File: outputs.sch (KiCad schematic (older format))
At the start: 51 parts, among them J2 USB_B_Micro, J3 HDMI_A_1.4, J4 FH26W-45S-0.3SHW(60), J5 Conn_02x16_Odd_Even, J6 Conn_01x02, Q1 AO3400, SW1 Up, SW2 Down, SW3 Left, SW4 Right, SW5 A, SW6 B, SW7 Select, SW8 Start, U10 NS8002

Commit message: Proto 1
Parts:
- renumbered C54 to C34, C36 to C35, C37 to C36, C38 to C37, C39 to C38, C40 to C39, C55 to C40, C56 to C44, C44 to C45, C45 to C46, C2 to C47, D2 to D3, D3 to D4, J6 to J3, J3 to J4, J4 to J5, J5 to J6, R14 to R25, R15 to R26, R16 to R27, R34 to R28, R17 to R29, R18 to R30, R35 to R31, R19 to R32, R20 to R33, R21 to R34, R22 to R35, R23 to R36, R24 to R37, R25 to R38, R26 to R39, R27 to R40, TP2 to TP12, TP3 to TP13, TP4 to TP14, TP5 to TP15
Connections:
- wire segments 161 -> 162
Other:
- note added: "Note: 100R is too little: the unit resets (5V overload?)"
- note added: "[38,39,40]=[im2,im1,im0]\n[0,0,0]=DBI type-B 18-bit"

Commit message: New design
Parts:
- added J10, J9: Conn_01x02_Male, Connector_PinHeader_2.54mm:PinHeader_1x02_P2.54mm_Vertical, symbol Connector:Conn_01x02_Male
- added J7, J8: Conn_02x03_Odd_Even, Connector_PinSocket_2.54mm:PinSocket_2x03_P2.54mm_Vertical, symbol Connector_Generic:Conn_02x03_Odd_Even
- SW1, SW2, SW3, SW4, SW5, SW6, SW7, SW8: footprint Button_Switch_THT:SW_PUSH_6mm -> Button_Switch_SMD:SW_Push_1P1T_NO_6x6mm_H9.5mm
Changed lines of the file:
@@
 EESchema Schematic File Version 4
 LIBS:hadbadge2019-cache
-EELAYER 26 0
+EELAYER 29 0
 EELAYER END
 $Descr A4 11693 8268
@@
 F 0 "SW1" H 9850 4300 50  0000 C CNN
 F 1 "Up" H 10150 4300 50  0000 C CNN
-F 2 "Button_Switch_THT:SW_PUSH_6mm" H 9350 4450 50  0001 C CNN
+F 2 "Button_Switch_SMD:SW_Push_1P1T_NO_6x6mm_H9.5mm" H 9350 4450 50  0001 C CNN
 F 3 "" H 9350 4450 50  0001 C CNN
 	1    9350 4250
@@
 F 0 "SW2" H 9850 4500 50  0000 C CNN
 F 1 "Down" H 10150 4500 50  0000 C CNN
-F 2 "Button_Switch_THT:SW_PUSH_6mm" H 9350 4650 50  0001 C CNN
+F 2 "Button_Switch_SMD:SW_Push_1P1T_NO_6x6mm_H9.5mm" H 9350 4650 50  0001 C CNN
 F 3 "" H 9350 4650 50  0001 C CNN
 	1    9350 4450
@@
 F 0 "SW3" H 9850 4700 50  0000 C CNN
 F 1 "Left" H 10150 4700 50  0000 C CNN
-F 2 "Button_Switch_THT:SW_PUSH_6mm" H 9350 4850 50  0001 C CNN
+F 2 "Button_Switch_SMD:SW_Push_1P1T_NO_6x6mm_H9.5mm" H 9350 4850 50  0001 C CNN
 F 3 "" H 9350 4850 50  0001 C CNN
 	1    9350 4650
@@
 F 0 "SW4" H 9850 4900 50  0000 C CNN
 F 1 "Right" H 10150 4900 50  0000 C CNN
-F 2 "Button_Switch_THT:SW_PUSH_6mm" H 9350 5050 50  0001 C CNN
+F 2 "Button_Switch_SMD:SW_Push_1P1T_NO_6x6mm_H9.5mm" H 9350 5050 50  0001 C CNN
 F 3 "" H 9350 5050 50  0001 C CNN
 	1    9350 4850
@@
 F 0 "SW5" H 9850 5100 50  0000 C CNN
 F 1 "A" H 10150 5100 50  0000 C CNN
-F 2 "Button_Switch_THT:SW_PUSH_6mm" H 9350 5250 50  0001 C CNN
+F 2 "Button_Switch_SMD:SW_Push_1P1T_NO_6x6mm_H9.5mm" H 9350 5250 50  0001 C CNN
 F 3 "" H 9350 5250 50  0001 C CNN
 	1    9350 5050
@@
 F 0 "SW6" H 9850 5300 50  0000 C CNN
 F 1 "B" H 10150 5300 50  0000 C CNN
-F 2 "Button_Switch_THT:SW_PUSH_6mm" H 9350 5450 50  0001 C CNN
+F 2 "Button_Switch_SMD:SW_Push_1P1T_NO_6x6mm_H9.5mm" H 9350 5450 50  0001 C CNN
 F 3 "" H 9350 5450 50  0001 C CNN
 	1    9350 5250
@@
 F 0 "SW7" H 9850 5500 50  0000 C CNN
 F 1 "Select" H 10150 5500 50  0000 C CNN
-F 2 "Button_Switch_THT:SW_PUSH_6mm" H 9350 5650 50  0001 C CNN
+F 2 "Button_Switch_SMD:SW_Push_1P1T_NO_6x6mm_H9.5mm" H 9350 5650 50  0001 C CNN
 F 3 "" H 9350 5650 50  0001 C CNN
 	1    9350 5450
@@
 F 0 "SW8" H 9850 5700 50  0000 C CNN
 F 1 "Start" H 10150 5700 50  0000 C CNN
-F 2 "Button_Switch_THT:SW_PUSH_6mm" H 9350 5850 50  0001 C CNN
+F 2 "Button_Switch_SMD:SW_Push_1P1T_NO_6x6mm_H9.5mm" H 9350 5850 50  0001 C CNN
 F 3 "" H 9350 5850 50  0001 C CNN
 	1    9350 5650
@@
 Text Notes 1550 2850 0    50   ~ 0
 Note: 100R is too little: the unit resets (5V overload?)
+$Comp
+L Connector_Generic:Conn_02x03_Odd_Even J7
+U 1 1 5CEDF19E
+P 4000 6700
+F 0 "J7" H 4050 7017 50  0000 C CNN
+F 1 "Conn_02x03_Odd_Even" H 4050 6926 50  0000 C CNN
+F 2 "Connector_PinSocket_2.54mm:PinSocket_2x03_P2.54mm_Vertical" H 4000 6700 50  0001 C CNN
+F 3 "~" H 4000 6700 50  0001 C CNN
+	1    4000 6700
+	1    0    0    -1
+$EndComp
+$Comp
+L Connector:Conn_01x02_Male J9
+U 1 1 5CEECB55
+P 3950 7100
+F 0 "J9" H 4058 7281 50  0000 C CNN
+F 1 "Conn_01x02_Male" H 4058 7190 50  0000 C CNN
+F 2 "Connector_PinHeader_2.54mm:PinHeader_1x02_P2.54mm_Vertical" H 3950 7100 50  0001 C CNN
+F 3 "~" H 3950 7100 50  0001 C CNN
+	1    3950 7100
+	1    0    0    -1
+$EndComp
+$Comp
+L Connector_Generic:Conn_02x03_Odd_Even J8
+U 1 1 5CEEDF6E
+P 5050 6700
+F 0 "J8" H 5100 7017 50  0000 C CNN
+F 1 "Conn_02x03_Odd_Even" H 5100 6926 50  0000 C CNN
+F 2 "Connector_PinSocket_2.54mm:PinSocket_2x03_P2.54mm_Vertical" H 5050 6700 50  0001 C CNN
+F 3 "~" H 5050 6700 50  0001 C CNN
+	1    5050 6700
+	1    0    0    -1
+$EndComp
+$Comp
+L Connector:Conn_01x02_Male J10
+U 1 1 5CEEDF74
+P 5000 7100
+F 0 "J10" H 5108 7281 50  0000 C CNN
+F 1 "Conn_01x02_Male" H 5108 7190 50  0000 C CNN
+F 2 "Connector_PinHeader_2.54mm:PinHeader_1x02_P2.54mm_Vertical" H 5000 7100 50  0001 C CNN
+F 3 "~" H 5000 7100 50  0001 C CNN
+	1    5000 7100
+	1    0    0    -1
+$EndComp
 $EndSCHEMATC

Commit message: WiP for proto 2
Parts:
- J6: footprint Connector_PinSocket_2.54mm:PinSocket_2x16_P2.54mm_Vertical -> Connector_PinSocket_2.54mm:PinSocket_2x16_P2.54mm_Horizontal
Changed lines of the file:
@@
 F 0 "J6" H 6100 5467 50  0000 C CNN
 F 1 "Conn_02x16_Odd_Even" H 6100 5376 50  0000 C CNN
-F 2 "Connector_PinSocket_2.54mm:PinSocket_2x16_P2.54mm_Vertical" H 6050 4550 50  0001 C CNN
+F 2 "Connector_PinSocket_2.54mm:PinSocket_2x16_P2.54mm_Horizontal" H 6050 4550 50  0001 C CNN
 F 3 "~" H 6050 4550 50  0001 C CNN
 	1    6050 4550

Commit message: Nearly done...
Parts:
- removed J6: Conn_02x16_Odd_Even, Connector_PinSocket_2.54mm:PinSocket_2x16_P2.54mm_Horizontal, symbol Connector_Generic:Conn_02x16_Odd_Even
- added J11: Conn_02x06_Odd_Even, Connector_PinSocket_2.54mm:PinSocket_2x06_P2.54mm_Horizontal, symbol Connector_Generic:Conn_02x06_Odd_Even
- added J6: Conn_02x20_Odd_Even, Connector_PinSocket_2.54mm:PinSocket_2x20_P2.54mm_Horizontal, symbol Connector_Generic:Conn_02x20_Odd_Even
- added R48, R49, R50, R51, R52, R53: 100, Resistor_SMD:R_0603_1608Metric, symbol Device:R
- J2: footprint JeroensFootprints:USB_Micro-B_0.8mm_taobao -> JeroensFootprints:USB_Micro-B_China_MK5P
- R33, R34, R35, R36, R37, R38: value 100 -> 180
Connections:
- net labels added: FLASH_CS_EXT, FLASH_HOLD, FLASH_MISO, FLASH_MOSI, FLASH_SCK, FLASH_WP, PMODA_1, PMODA_2, PMODA_3, PMODA_4, PMODB_1, PMODB_2, PMODB_3, PMODB_4, SAO1_DRM, SAO1_GPIO1, SAO1_GPIO2, SAO1_GPIO3, SAO1_SCL, SAO1_SDA, SAO2_DRM, SAO2_GPIO1, SAO2_GPIO2, SAO2_GPIO3, SAO2_SCL, SAO2_SDA
- wire segments 162 -> 174
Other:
- moved on the sheet: J10, J8, J9

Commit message: Proto2, final version
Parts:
- added J12: Conn_02x06_Odd_Even, Connector_PinSocket_2.54mm:PinSocket_2x06_P2.54mm_Horizontal, symbol Connector_Generic:Conn_02x06_Odd_Even
- D3, D4: value D_Zener -> 3V6; footprint Diode_SMD:D_0603_1608Metric -> Diode_SMD:D_SOD-323; Notes (none) -> SOD323 zener, eg MM3Z3V6
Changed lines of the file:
@@
 P 2800 2100
 F 0 "D3" V 2650 2150 50  0000 L CNN
-F 1 "D_Zener" V 2800 2400 50  0000 L CNN
-F 2 "Diode_SMD:D_0603_1608Metric" H 2800 2100 50  0001 C CNN
+F 1 "3V6" V 2800 2400 50  0000 L CNN
+F 2 "Diode_SMD:D_SOD-323" H 2800 2100 50  0001 C CNN
 F 3 "~" H 2800 2100 50  0001 C CNN
+F 4 "SOD323 zener, eg MM3Z3V6" H 2800 2100 50  0001 C CNN "Notes"
 	1    2800 2100
 	0    1    1    0
@@
 P 3000 2100
 F 0 "D4" V 2850 2150 50  0000 L CNN
-F 1 "D_Zener" V 3100 2200 50  0000 L CNN
-F 2 "Diode_SMD:D_0603_1608Metric" H 3000 2100 50  0001 C CNN
+F 1 "3V6" V 3100 2200 50  0000 L CNN
+F 2 "Diode_SMD:D_SOD-323" H 3000 2100 50  0001 C CNN
 F 3 "~" H 3000 2100 50  0001 C CNN
+F 4 "SOD323 zener, eg MM3Z3V6" H 3000 2100 50  0001 C CNN "Notes"
 	1    3000 2100
 	0    1    1    0
@@
 Wire Wire Line
 	6300 4900 6900 4900
+$Comp
+L Connector_Generic:Conn_02x06_Odd_Even J12
+U 1 1 5DC51358
+P 7100 5900
+F 0 "J12" H 7150 6317 50  0000 C CNN
+F 1 "Conn_02x06_Odd_Even" H 7150 6226 50  0000 C CNN
+F 2 "Connector_PinSocket_2.54mm:PinSocket_2x06_P2.54mm_Horizontal" H 7100 5900 50  0001 C CNN
+F 3 "~" H 7100 5900 50  0001 C CNN
+	1    7100 5900
+	1    0    0    -1
+$EndComp
 $EndSCHEMATC

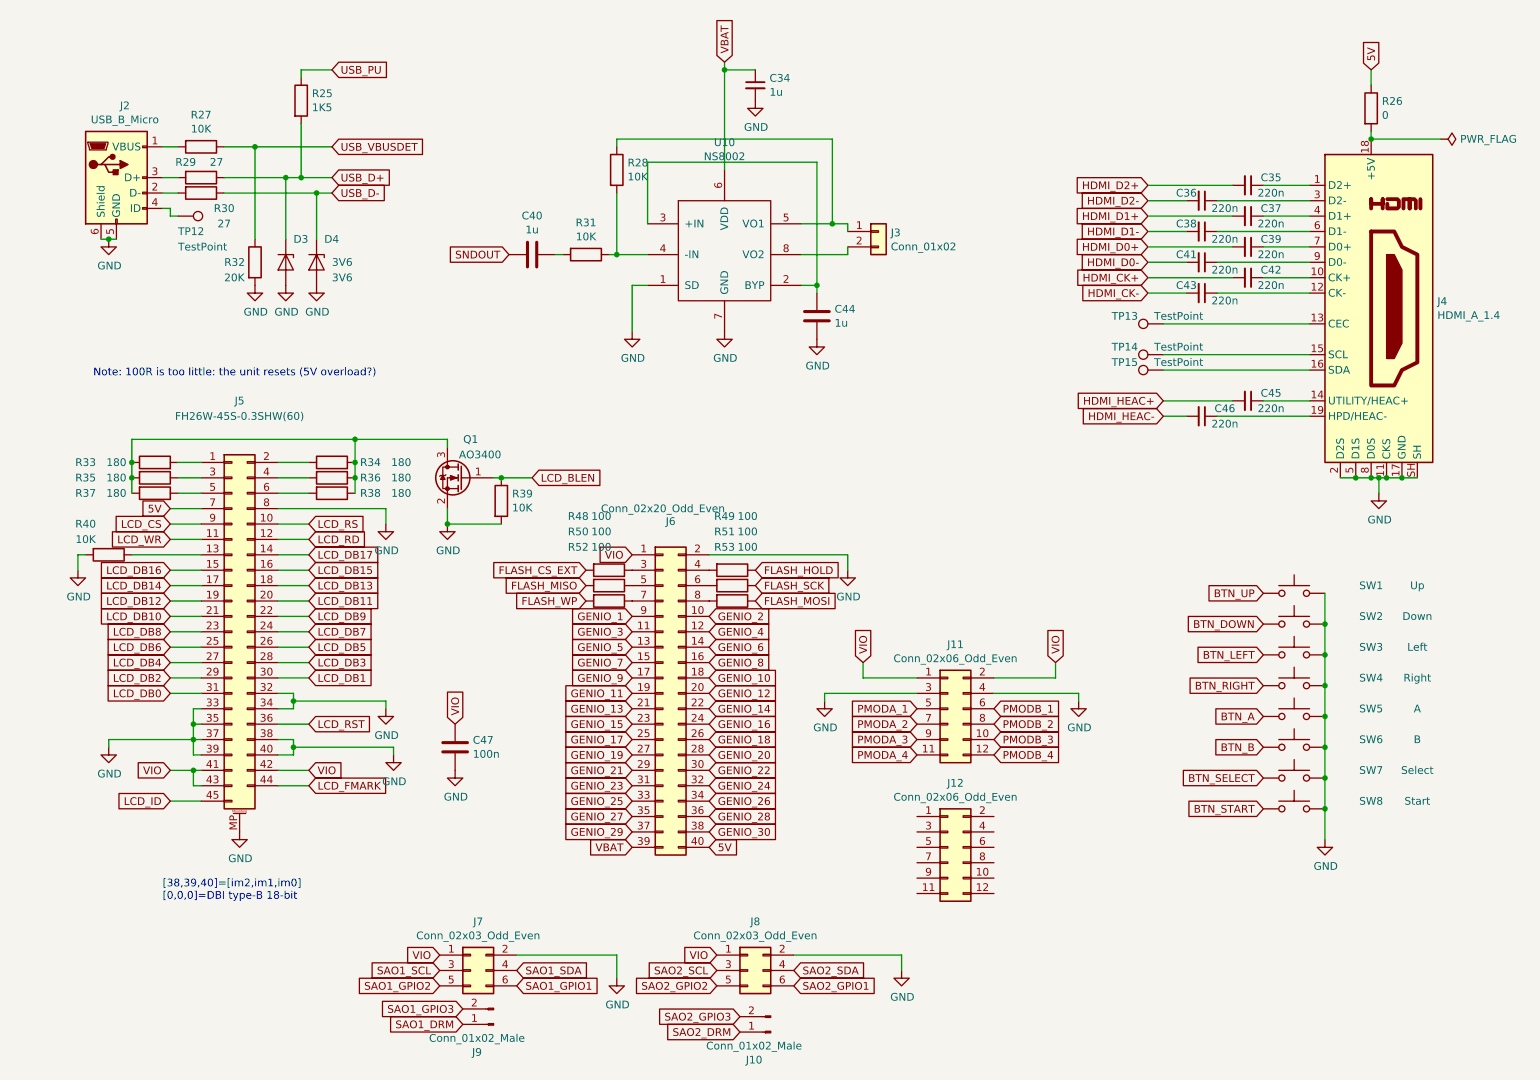
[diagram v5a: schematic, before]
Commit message: Fix fab drawings to make sense
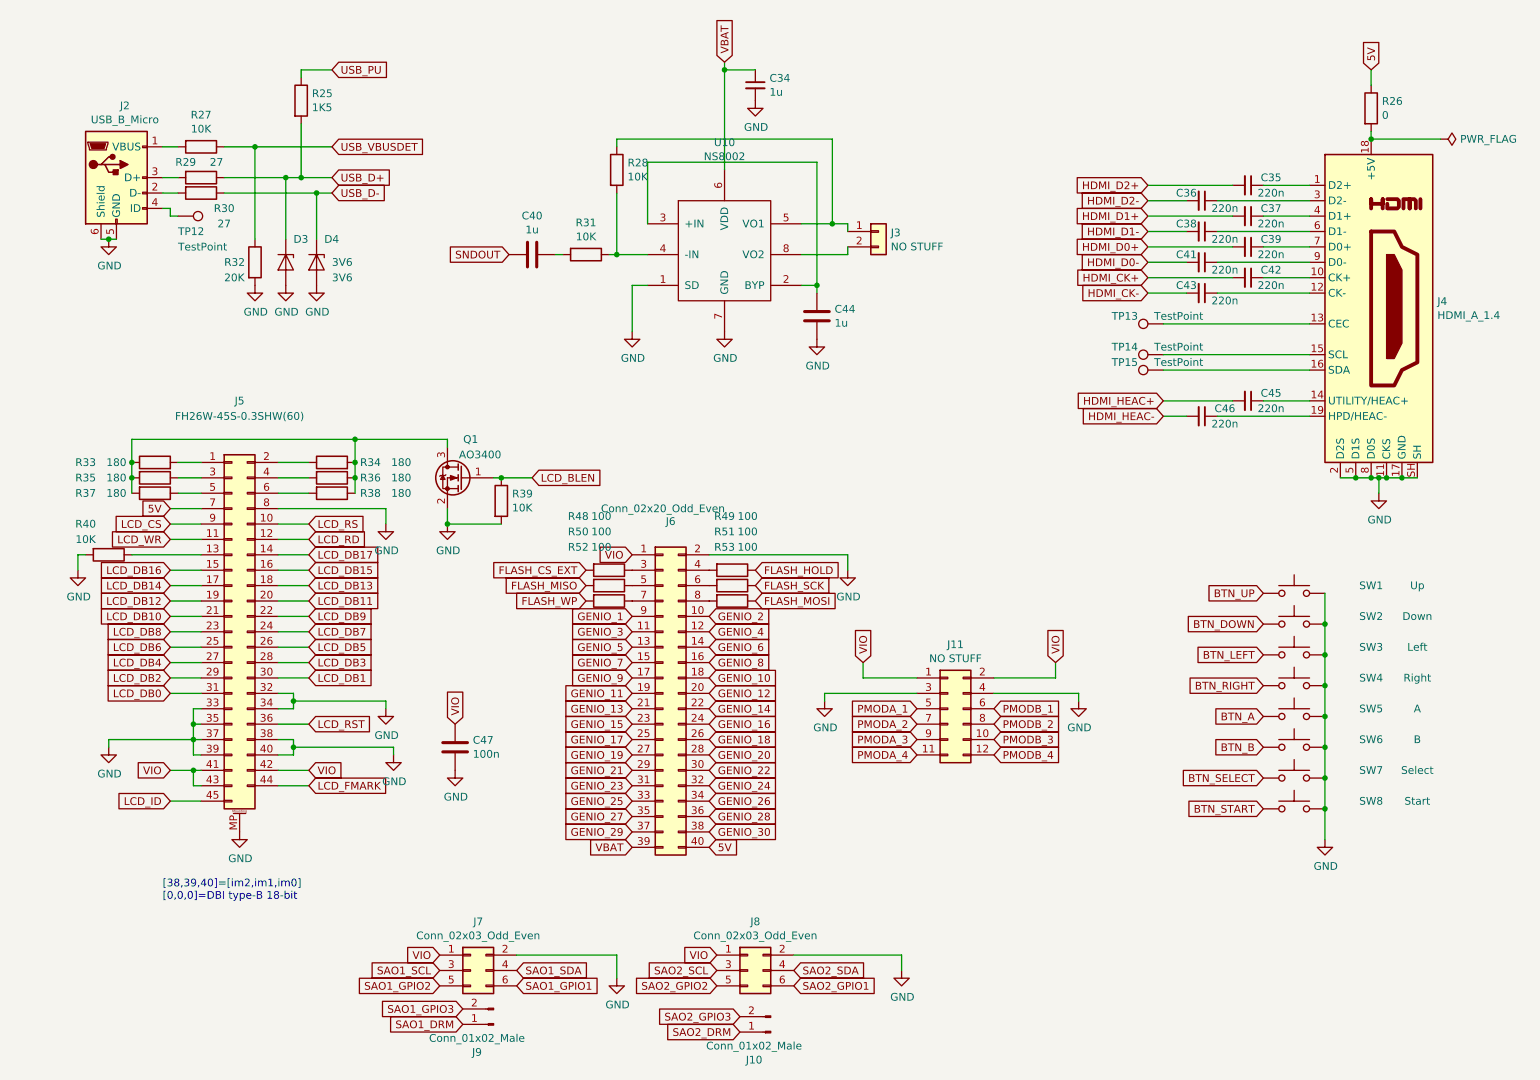
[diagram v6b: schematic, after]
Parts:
- removed J12: Conn_02x06_Odd_Even, Connector_PinSocket_2.54mm:PinSocket_2x06_P2.54mm_Horizontal, symbol Connector_Generic:Conn_02x06_Odd_Even
- J11: value Conn_02x06_Odd_Even -> NO STUFF; Notes (none) -> NO STUFF
- J3: value Conn_01x02 -> NO STUFF; Notes (none) -> NO STUFF
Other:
- note removed: "Note: 100R is too little: the unit resets (5V overload?)"
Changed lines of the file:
@@
 P 6650 1900
 F 0 "J3" H 6730 1892 50  0000 L CNN
-F 1 "Conn_01x02" H 6730 1801 50  0000 L CNN
+F 1 "NO STUFF" H 6730 1801 50  0000 L CNN
 F 2 "Connector_PinSocket_2.54mm:PinSocket_1x02_P2.54mm_Vertical" H 6650 1900 50  0001 C CNN
 F 3 "~" H 6650 1900 50  0001 C CNN
+F 4 "NO STUFF" H 6650 1900 50  0001 C CNN "Notes"
 	1    6650 1900
 	1    0    0    -1
@@
 Text Notes 2000 6250 0    50   ~ 0
 [38,39,40]=[im2,im1,im0]\n[0,0,0]=DBI type-B 18-bit
-Text Notes 1550 2850 0    50   ~ 0
-Note: 100R is too little: the unit resets (5V overload?)
 $Comp
 L Connector_Generic:Conn_02x03_Odd_Even J7
@@
 P 7100 5000
 F 0 "J11" H 7150 5417 50  0000 C CNN
-F 1 "Conn_02x06_Odd_Even" H 7150 5326 50  0000 C CNN
+F 1 "NO STUFF" H 7150 5326 50  0000 C CNN
 F 2 "Connector_PinSocket_2.54mm:PinSocket_2x06_P2.54mm_Horizontal" H 7100 5000 50  0001 C CNN
 F 3 "~" H 7100 5000 50  0001 C CNN
+F 4 "NO STUFF" H 7100 5000 50  0001 C CNN "Notes"
 	1    7100 5000
 	1    0    0    -1
@@
 Wire Wire Line
 	6300 4900 6900 4900
-$Comp
-L Connector_Generic:Conn_02x06_Odd_Even J12
-U 1 1 5DC51358
-P 7100 5900
-F 0 "J12" H 7150 6317 50  0000 C CNN
-F 1 "Conn_02x06_Odd_Even" H 7150 6226 50  0000 C CNN
-F 2 "Connector_PinSocket_2.54mm:PinSocket_2x06_P2.54mm_Horizontal" H 7100 5900 50  0001 C CNN
-F 3 "~" H 7100 5900 50  0001 C CNN
-	1    7100 5900
-	1    0    0    -1
-$EndComp
 $EndSCHEMATC

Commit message: This is proto 3.
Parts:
- added C49, C51: 100n, Capacitor_SMD:C_0603_1608Metric, symbol Device:C_Small
- added C50: 10u, Capacitor_SMD:C_0805_2012Metric, symbol Device:C_Small
- added J12: NO STUFF, Connector_PinHeader_2.54mm:PinHeader_1x04_P2.54mm_Vertical, symbol Connector:Conn_01x04_Female
- added R68: 10K, Resistor_SMD:R_0603_1608Metric, symbol Device:R
- added U12: RPM973, lib:RPM973-H11, symbol RPM973:RPM973
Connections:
- net GND: now also C49.2, C50.2, C51.2, J12.4 (Pin_4), U12.7 (GND), U12.SH (SHIELD)
- net VBAT: now also C49.1, U12.1 (LEDA)
- net VIO: now also C50.1, C51.1, R68.1, U12.5 (VCC), U12.6 (VIO)
- net at J2.1 (VBUS), R27.2: now also J12.1 (Pin_1)
- net at J2.2 (D-), R30.2: now also J12.2 (Pin_2)
- net at J2.3 (D+), R29.2: now also J12.3 (Pin_3)
- new net IRDA_RX: U12.3 (RXD)
- new net IRDA_SD: R68.2, U12.4 (PWDWN)
- new net IRDA_TX: U12.2 (TXD)
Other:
- note added: "Amplifier; user can connect\nspeaker to J3 for audio."
- note added: "J12 is the 'Header of Shame'. If someone\nrips off the USB connector, they can always\ncut off a cable and solder it to J12."
- moved on the sheet: D3, D4, J11, J2, R25, R27, R29, R30, R32, TP12

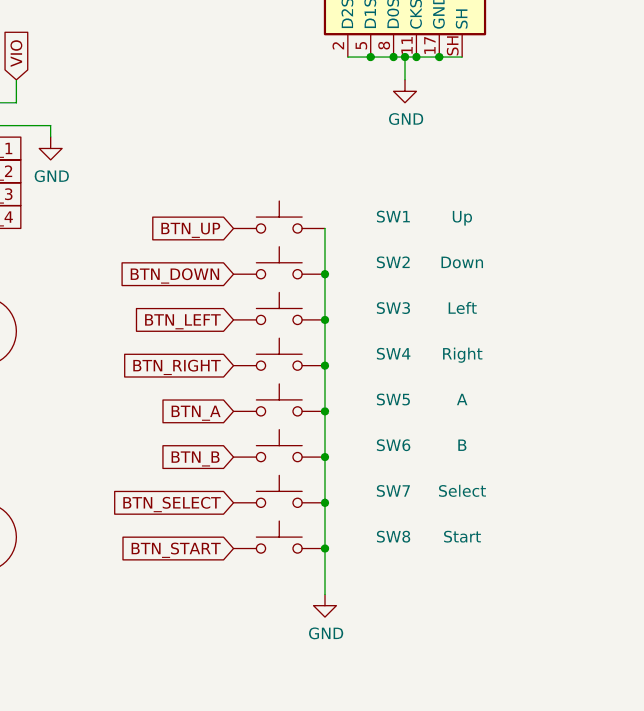
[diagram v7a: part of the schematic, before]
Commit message: Final changes: add some fiducials, clean up vias. Ready for prod, I hope.
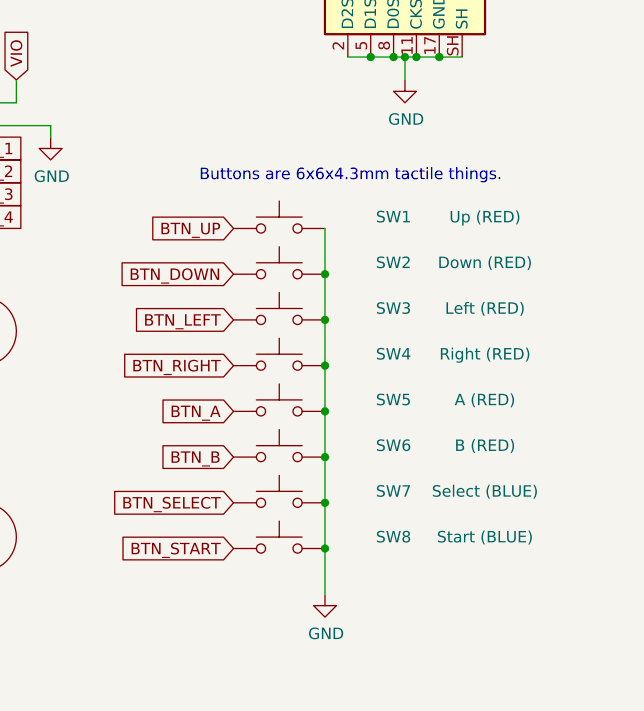
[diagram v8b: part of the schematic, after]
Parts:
- SW1: value Up -> Up (RED)
- SW2: value Down -> Down (RED)
- SW3: value Left -> Left (RED)
- SW4: value Right -> Right (RED)
- SW5: value A -> A (RED)
- SW6: value B -> B (RED)
- SW7: value Select -> Select (BLUE)
- SW8: value Start -> Start (BLUE)
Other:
- note added: "Buttons are 6x6x4.3mm tactile things."
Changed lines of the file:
@@
 P 9350 4250
 F 0 "SW1" H 9850 4300 50  0000 C CNN
-F 1 "Up" H 10150 4300 50  0000 C CNN
+F 1 "Up (RED)" H 10250 4300 50  0000 C CNN
 F 2 "Button_Switch_SMD:SW_Push_1P1T_NO_6x6mm_H9.5mm" H 9350 4450 50  0001 C CNN
-F 3 "" H 9350 4450 50  0001 C CNN
+F 3 "https://item.taobao.com/item.htm?id=40750516732" H 9350 4450 50  0001 C CNN
 	1    9350 4250
 	1    0    0    -1
@@
 P 9350 4450
 F 0 "SW2" H 9850 4500 50  0000 C CNN
-F 1 "Down" H 10150 4500 50  0000 C CNN
+F 1 "Down (RED)" H 10250 4500 50  0000 C CNN
 F 2 "Button_Switch_SMD:SW_Push_1P1T_NO_6x6mm_H9.5mm" H 9350 4650 50  0001 C CNN
-F 3 "" H 9350 4650 50  0001 C CNN
+F 3 "https://item.taobao.com/item.htm?id=40750516732" H 9350 4650 50  0001 C CNN
 	1    9350 4450
 	1    0    0    -1
@@
 P 9350 4650
 F 0 "SW3" H 9850 4700 50  0000 C CNN
-F 1 "Left" H 10150 4700 50  0000 C CNN
+F 1 "Left (RED)" H 10250 4700 50  0000 C CNN
 F 2 "Button_Switch_SMD:SW_Push_1P1T_NO_6x6mm_H9.5mm" H 9350 4850 50  0001 C CNN
-F 3 "" H 9350 4850 50  0001 C CNN
+F 3 "https://item.taobao.com/item.htm?id=40750516732" H 9350 4850 50  0001 C CNN
 	1    9350 4650
 	1    0    0    -1
@@
 P 9350 4850
 F 0 "SW4" H 9850 4900 50  0000 C CNN
-F 1 "Right" H 10150 4900 50  0000 C CNN
+F 1 "Right (RED)" H 10250 4900 50  0000 C CNN
 F 2 "Button_Switch_SMD:SW_Push_1P1T_NO_6x6mm_H9.5mm" H 9350 5050 50  0001 C CNN
-F 3 "" H 9350 5050 50  0001 C CNN
+F 3 "https://item.taobao.com/item.htm?id=40750516732" H 9350 5050 50  0001 C CNN
 	1    9350 4850
 	1    0    0    -1
@@
 P 9350 5050
 F 0 "SW5" H 9850 5100 50  0000 C CNN
-F 1 "A" H 10150 5100 50  0000 C CNN
+F 1 "A (RED)" H 10250 5100 50  0000 C CNN
 F 2 "Button_Switch_SMD:SW_Push_1P1T_NO_6x6mm_H9.5mm" H 9350 5250 50  0001 C CNN
-F 3 "" H 9350 5250 50  0001 C CNN
+F 3 "https://item.taobao.com/item.htm?id=40750516732" H 9350 5250 50  0001 C CNN
 	1    9350 5050
 	1    0    0    -1
@@
 P 9350 5250
 F 0 "SW6" H 9850 5300 50  0000 C CNN
-F 1 "B" H 10150 5300 50  0000 C CNN
+F 1 "B (RED)" H 10250 5300 50  0000 C CNN
 F 2 "Button_Switch_SMD:SW_Push_1P1T_NO_6x6mm_H9.5mm" H 9350 5450 50  0001 C CNN
-F 3 "" H 9350 5450 50  0001 C CNN
+F 3 "https://item.taobao.com/item.htm?id=40750516732" H 9350 5450 50  0001 C CNN
 	1    9350 5250
 	1    0    0    -1
@@
 P 9350 5450
 F 0 "SW7" H 9850 5500 50  0000 C CNN
-F 1 "Select" H 10150 5500 50  0000 C CNN
+F 1 "Select (BLUE)" H 10250 5500 50  0000 C CNN
 F 2 "Button_Switch_SMD:SW_Push_1P1T_NO_6x6mm_H9.5mm" H 9350 5650 50  0001 C CNN
-F 3 "" H 9350 5650 50  0001 C CNN
+F 3 "https://item.taobao.com/item.htm?id=40750516732" H 9350 5650 50  0001 C CNN
 	1    9350 5450
 	1    0    0    -1
@@
 P 9350 5650
 F 0 "SW8" H 9850 5700 50  0000 C CNN
-F 1 "Start" H 10150 5700 50  0000 C CNN
+F 1 "Start (BLUE)" H 10250 5700 50  0000 C CNN
 F 2 "Button_Switch_SMD:SW_Push_1P1T_NO_6x6mm_H9.5mm" H 9350 5850 50  0001 C CNN
-F 3 "" H 9350 5850 50  0001 C CNN
+F 3 "https://item.taobao.com/item.htm?id=40750516732" H 9350 5850 50  0001 C CNN
 	1    9350 5650
 	1    0    0    -1
@@
 Text Notes 1100 1150 0    50   ~ 0
 J12 is the 'Header of Shame'. If someone\nrips off the USB connector, they can always\ncut off a cable and solder it to J12.
+Text Notes 9000 4050 0    50   ~ 0
+Buttons are 6x6x4.3mm tactile things.
 $EndSCHEMATC
